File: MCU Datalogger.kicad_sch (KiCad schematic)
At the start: 25 parts, among them U1 24LC1025, U2 24LC1025, U3 DS1337S_, U4 ATMEGA328P-AU, Y1 Crystal, Y2 Crystal

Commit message: Added component values.
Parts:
- C1, C4: value C -> 0.1uF
- C2, C3: value C -> 22pF
- C5: value C_Polarized -> 100nF
- R1, R2: value R -> 4.7K
- R3, R4, R5: value R -> 10K
- R7: value R -> 330
- Y1: value Crystal -> 16 MHz
- Y2: value Crystal -> 32.768 KHz
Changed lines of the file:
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@@
 			)
 		)
-		(property "Value" "R"
+		(property "Value" "10K"
 			(at 106.68 39.3699 0)
 			(effects
@@
 			)
 		)
+		(property "Purpose" ""
+			(at 104.14 38.1 0)
+			(effects
+				(font
+					(size 1.27 1.27)
+				)
+			)
+		)
 		(pin "1"
 		)
@@
 			)
 		)
-		(property "Value" "Crystal"
+		(property "Value" "16 MHz"
 			(at 168.91 52.0699 90)
 			(effects
@@
 			)
 		)
+		(property "Purpose" ""
+			(at 165.1 50.8 0)
+			(effects
+				(font
+					(size 1.27 1.27)
+				)
+			)
+		)
 		(pin "1"
 		)
@@
 			)
 		)
-		(property "Value" "R"
+		(property "Value" "4.7K"
 			(at 99.06 132.0799 0)
 			(effects
@@
 			)
 		)
+		(property "Purpose" ""
+			(at 96.52 130.81 0)
+			(effects
+				(font
+					(size 1.27 1.27)
+				)
+			)
+		)
 		(pin "2"
 		)
@@
 			)
 		)
-		(property "Value" "Crystal"
+		(property "Value" "32.768 KHz"
 			(at 29.21 44.4499 90)
 			(effects
@@
 			)
 		)
+		(property "Purpose" ""
+			(at 25.4 43.18 0)
+			(effects
+				(font
+					(size 1.27 1.27)
+				)
+			)
+		)
 		(pin "1"
 		)
@@
 			)
 		)
-		(property "Value" "R"
+		(property "Value" "330"
 			(at 246.38 57.1499 0)
 			(effects
@@
 			)
 		)
+		(property "Purpose" ""
+			(at 243.84 55.88 0)
+			(effects
+				(font
+					(size 1.27 1.27)
+				)
+			)
+		)
 		(pin "1"
 		)
@@
 			)
 		)
-		(property "Value" "R"
+		(property "Value" "10K"
 			(at 99.06 39.3699 0)
 			(effects
@@
 			)
 		)
+		(property "Purpose" ""
+			(at 96.52 38.1 0)
+			(effects
+				(font
+					(size 1.27 1.27)
+				)
+			)
+		)
 		(pin "1"
 		)
@@
 			)
 		)
-		(property "Value" "C"
+		(property "Value" "0.1uF"
 			(at 118.11 41.9099 0)
 			(effects
@@
 			)
 		)
+		(property "Purpose" ""
+			(at 114.3 40.64 0)
+			(effects
+				(font
+					(size 1.27 1.27)
+				)
+			)
+		)
 		(pin "1"
 		)
@@
 			)
 		)
-		(property "Value" "C_Polarized"
+		(property "Value" "100nF"
 			(at 257.81 32.1309 0)
 			(effects
@@
 			)
 		)
+		(property "Purpose" ""
+			(at 254 31.75 0)
+			(effects
+				(font
+					(size 1.27 1.27)
+				)
+			)
+		)
 		(pin "2"
 		)
@@
 			)
 		)
-		(property "Value" "C"
+		(property "Value" "0.1uF"
 			(at 165.1 15.24 90)
 			(effects
@@
 			)
 		)
+		(property "Purpose" ""
+			(at 165.1 20.32 0)
+			(effects
+				(font
+					(size 1.27 1.27)
+				)
+			)
+		)
 		(pin "2"
 		)
@@
 			)
 		)
-		(property "Value" "R"
+		(property "Value" "10K"
 			(at 166.37 72.39 90)
 			(effects
@@
 			)
 		)
+		(property "Purpose" ""
+			(at 166.37 76.2 0)
+			(effects
+				(font
+					(size 1.27 1.27)
+				)
+			)
+		)
 		(pin "1"
 		)
@@
 			)
 		)
-		(property "Value" "R"
+		(property "Value" "4.7K"
 			(at 106.68 132.0799 0)
 			(effects
@@
 			)
 		)
+		(property "Purpose" ""
+			(at 104.14 130.81 0)
+			(effects
+				(font
+					(size 1.27 1.27)
+				)
+			)
+		)
 		(pin "1"
 		)
@@
 			)
 		)
-		(property "Value" "C"
+		(property "Value" "22pF"
 			(at 151.13 50.7999 0)
 			(effects
@@
 			)
 		)
+		(property "Purpose" ""
+			(at 147.32 49.53 0)
+			(effects
+				(font
+					(size 1.27 1.27)
+				)
+			)
+		)
 		(pin "1"
 		)
@@
 			)
 		)
-		(property "Value" "C"
+		(property "Value" "22pF"
 			(at 151.13 68.5799 0)
 			(effects
@@
 			)
 		)
+		(property "Purpose" ""
+			(at 147.32 67.31 0)
+			(effects
+				(font
+					(size 1.27 1.27)
+				)
+			)
+		)

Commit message: Completed symbol-footprint associations.
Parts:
- BT1: footprint (none) -> Connector_PinHeader_2.54mm:PinHeader_1x01_P2.54mm_Vertical
- C1, C2, C3, C4, C5: footprint (none) -> Capacitor_SMD:C_0805_2012Metric
- D1, D2: footprint (none) -> LED_SMD:LED_0805_2012Metric
- H1, H2, H3, H4: footprint (none) -> MountingHole:MountingHole_2.1mm
- R1, R2, R3, R4, R5, R7: footprint (none) -> Resistor_SMD:R_0805_2012Metric
- R6: value R -> 330; footprint (none) -> Resistor_SMD:R_0805_2012Metric
- U1, U2: footprint (none) -> Package_SO:SSOP-8_5.25x5.24mm_P1.27mm
- U3: footprint DS1337S_:SOIC127P600X175-8N -> MCU Datalogger:SOIC127P600X175-8N
- U4: footprint ATMEGA328P-AU:QFP80P900X900X120-32N -> MCU Datalogger:QFP80P900X900X120-32N
- Y1, Y2: footprint (none) -> Crystal:Crystal_SMD_5032-2Pin_5.0x3.2mm_HandSoldering
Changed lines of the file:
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@@
 			)
 		)
-		(property "Footprint" ""
+		(property "Footprint" "Resistor_SMD:R_0805_2012Metric"
 			(at 102.362 38.1 90)
 			(effects
@@
 			)
 		)
-		(property "Footprint" ""
+		(property "Footprint" "MountingHole:MountingHole_2.1mm"
 			(at 208.28 134.62 0)
 			(effects
@@
 			)
 		)
-		(property "Footprint" "ATMEGA328P-AU:QFP80P900X900X120-32N"
+		(property "Footprint" "MCU Datalogger:QFP80P900X900X120-32N"
 			(at 210.82 48.26 0)
 			(effects
@@
 			)
 		)
-		(property "Footprint" ""
+		(property "Footprint" "Crystal:Crystal_SMD_5032-2Pin_5.0x3.2mm_HandSoldering"
 			(at 165.1 50.8 0)
 			(effects
@@
 			)
 		)
-		(property "Footprint" ""
+		(property "Footprint" "Resistor_SMD:R_0805_2012Metric"
 			(at 94.742 130.81 90)
 			(effects
@@
 			)
 		)
-		(property "Footprint" ""
+		(property "Footprint" "Crystal:Crystal_SMD_5032-2Pin_5.0x3.2mm_HandSoldering"
 			(at 25.4 43.18 0)
 			(effects
@@
 			)
 		)
-		(property "Footprint" ""
+		(property "Footprint" "Resistor_SMD:R_0805_2012Metric"
 			(at 242.062 55.88 90)
 			(effects
@@
 			)
 		)
-		(property "Value" "R"
+		(property "Value" "330"
 			(at 148.59 29.21 90)
 			(effects
@@
 			)
 		)
-		(property "Footprint" ""
+		(property "Footprint" "Resistor_SMD:R_0805_2012Metric"
 			(at 148.59 34.798 90)
 			(effects
@@
 			)
 		)
+		(property "Purpose" ""
+			(at 148.59 33.02 0)
+			(effects
+				(font
+					(size 1.27 1.27)
+				)
+			)
+		)
 		(pin "2"
 		)
@@
 			)
 		)
-		(property "Footprint" "DS1337S_:SOIC127P600X175-8N"
+		(property "Footprint" "MCU Datalogger:SOIC127P600X175-8N"
 			(at 66.04 43.18 0)
 			(effects
@@
 			)
 		)
-		(property "Footprint" ""
+		(property "Footprint" "Resistor_SMD:R_0805_2012Metric"
 			(at 94.742 38.1 90)
 			(effects
@@
 			)
 		)
-		(property "Footprint" ""
+		(property "Footprint" "Capacitor_SMD:C_0805_2012Metric"
 			(at 115.2652 44.45 0)
 			(effects
@@
 			)
 		)
-		(property "Footprint" ""
+		(property "Footprint" "MountingHole:MountingHole_2.1mm"
 			(at 208.28 139.7 0)
 			(effects
@@
 			)
 		)
-		(property "Footprint" ""
+		(property "Footprint" "Capacitor_SMD:C_0805_2012Metric"
 			(at 254.9652 35.56 0)
 			(effects
@@
 			)
 		)
-		(property "Footprint" ""
+		(property "Footprint" "Capacitor_SMD:C_0805_2012Metric"
 			(at 168.91 19.3548 0)
 			(effects
@@
 			)
 		)
-		(property "Footprint" ""
+		(property "Footprint" "Resistor_SMD:R_0805_2012Metric"
 			(at 166.37 74.422 90)
 			(effects
@@
 			)
 		)
-		(property "Footprint" ""
+		(property "Footprint" "MountingHole:MountingHole_2.1mm"
 			(at 208.28 124.46 0)
 			(effects
@@
 			)
 		)
-		(property "Footprint" ""
+		(property "Footprint" "Package_SO:SSOP-8_5.25x5.24mm_P1.27mm"
 			(at 71.12 129.54 0)
 			(effects
@@
 			)
 		)
-		(property "Footprint" ""
+		(property "Footprint" "LED_SMD:LED_0805_2012Metric"
 			(at 243.84 40.64 0)
 			(effects
@@
 			)
 		)
-		(property "Footprint" ""
+		(property "Footprint" "MountingHole:MountingHole_2.1mm"
 			(at 208.28 129.54 0)
 			(effects
@@
 			)
 		)
-		(property "Footprint" ""
+		(property "Footprint" "Connector_PinHeader_2.54mm:PinHeader_1x01_P2.54mm_Vertical"
 			(at 271.78 28.956 90)
 			(effects
@@
 			)
 		)
-		(property "Footprint" ""
+		(property "Footprint" "Resistor_SMD:R_0805_2012Metric"
 			(at 102.362 130.81 90)
 			(effects
@@
 			)
 		)
-		(property "Footprint" ""
+		(property "Footprint" "Capacitor_SMD:C_0805_2012Metric"
 			(at 148.2852 53.34 0)
 			(effects
@@
 			)
 		)
-		(property "Footprint" ""
+		(property "Footprint" "Package_SO:SSOP-8_5.25x5.24mm_P1.27mm"
 			(at 43.18 129.54 0)
 			(effects
@@
 			)
 		)
-		(property "Footprint" ""
+		(property "Footprint" "Capacitor_SMD:C_0805_2012Metric"
 			(at 148.2852 71.12 0)
 			(effects
@@
 			)
 		)
-		(property "Footprint" ""
+		(property "Footprint" "LED_SMD:LED_0805_2012Metric"
 			(at 167.64 33.02 0)
 			(effects

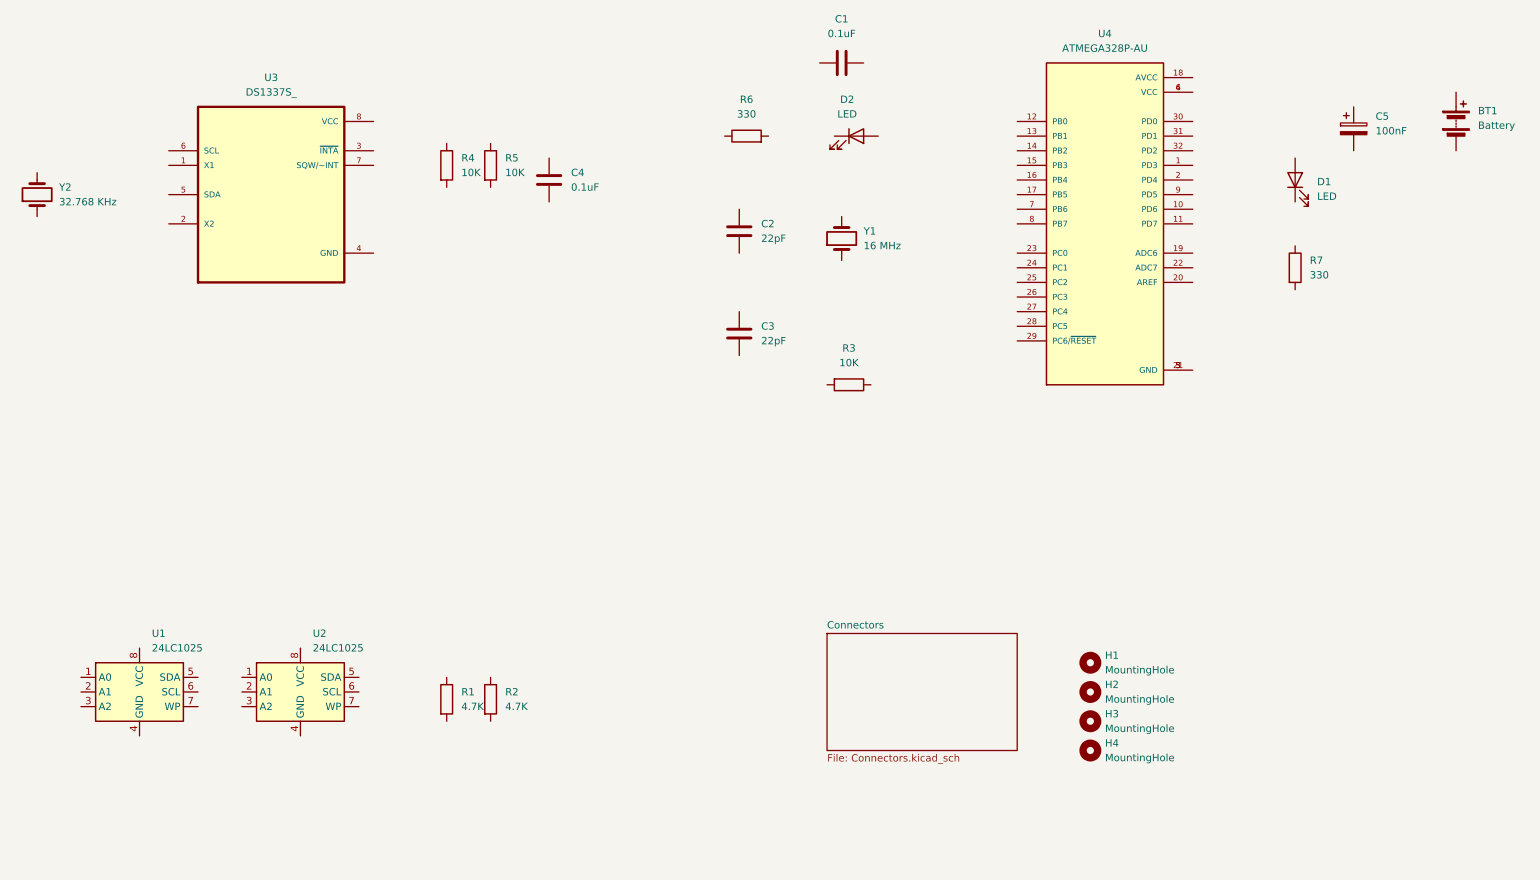
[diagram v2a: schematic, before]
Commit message: Completed wiring of main sheet.
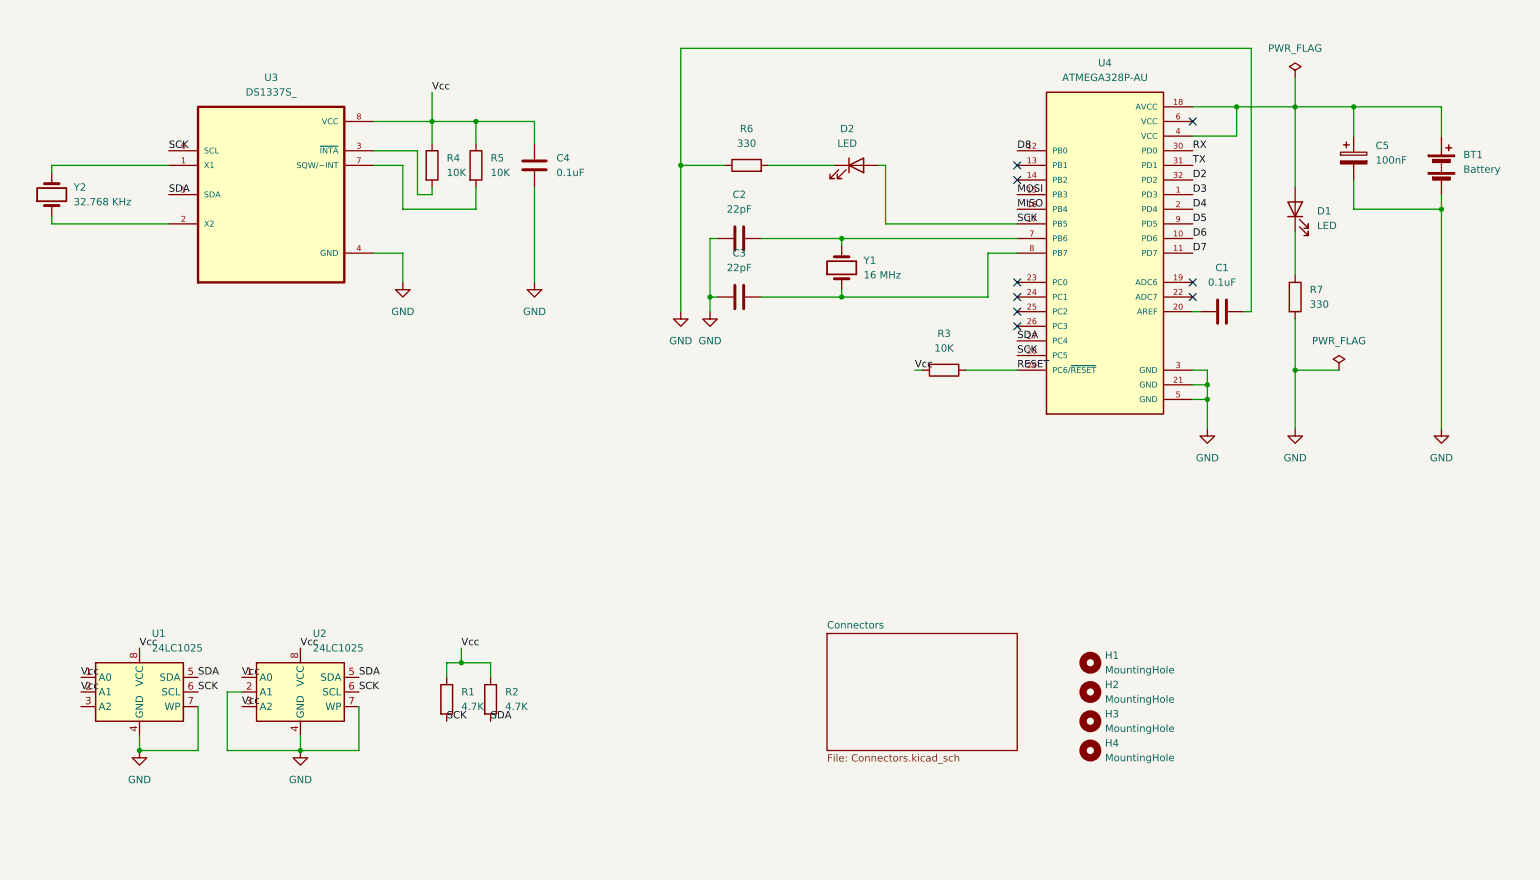
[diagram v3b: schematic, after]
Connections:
- net Vcc: now reaches R5.1
- net Vcc: now also C4.1, R1.1, R2.1, R3.2, R4.1, U1.1 (A0), U1.2 (A1), U1.8 (VCC), U2.1 (A0), U2.3 (A2), U2.8 (VCC), U3.8 (VCC)
- net at R5.2: now also U3.7 (SQW/~INT)
- net D3: now reaches U4.1 (PD3)
- net D6: now reaches U4.10 (PD6)
- net D7: now reaches U4.11 (PD7)
- net D8: now reaches U4.12 (PB0)
- net MOSI: now reaches U4.15 (PB3)
- net MISO: now reaches U4.16 (PB4)
- net SCK: now reaches U4.17 (PB5)
- net SCK: now also D2.2 (A), R1.2, U1.6 (SCL), U2.6 (SCL), U3.6 (SCL), U4.28 (PC5)
- net at U4.18 (AVCC): now also BT1.1 (+), C5.1, D1.2 (A), U4.4 (VCC)
- net D4: now reaches U4.2 (PD4)
- net at U4.20 (AREF): now also C1.1
- net GND: now reaches U4.21 (GND), U4.3 (GND), U4.5 (GND)
- net GND: now also BT1.2 (-), C1.2, C2.1, C3.1, C4.2, C5.2, R6.1, R7.2, U1.4 (GND), U1.7 (WP), U2.2 (A1), U2.4 (GND), U2.7 (WP), U3.4 (GND)
- net SDA: now reaches U4.27 (PC4)
- net SDA: now also R2.2, U1.5 (SDA), U2.5 (SDA), U3.5 (SDA)
- net RESET: now reaches U4.29 (PC6/~{RESET})
- net RESET: now also R3.1
- net RX: now reaches U4.30 (PD0)
- net TX: now reaches U4.31 (PD1)
- net D2: now reaches U4.32 (PD2)
- net at U4.6 (VCC): no longer U4.4 (VCC)
- net at U4.7 (PB6): now also C2.2, Y1.2
- net at U4.8 (PB7): now also C3.2, Y1.1
- net D5: now reaches U4.9 (PD5)
- net at Y2.1: now also U3.2 (X2)
- net at Y2.2: now also U3.1 (X1)
- net at R7.1: now also D1.1 (K)
- net at R6.2: now also D2.1 (K)
- net at U3.3 (~{INTA}): now also R4.2
- no-connect marks 0 -> 9
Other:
- moved on the sheet: BT1, C1, C2, C3, C4, C5, D1, D2, R3, R4, R5, R6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

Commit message: Completed wiring in the second sheet.
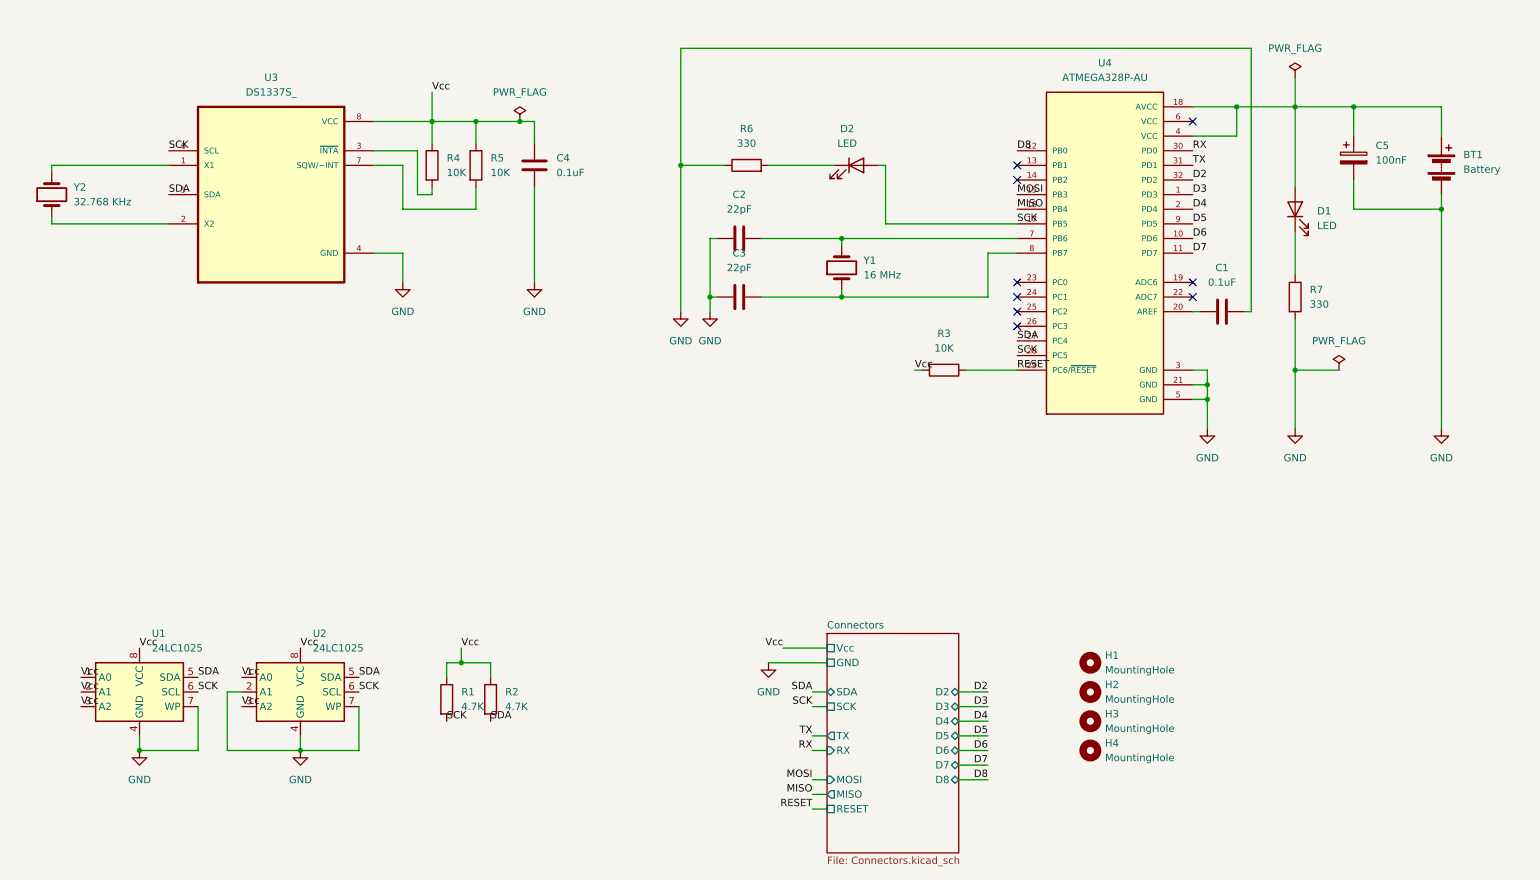
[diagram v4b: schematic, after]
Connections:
- net Vcc: now also U1.3 (A2)
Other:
- sheet Connectors ports: added D2, D3, D4, D5, D6, D7, D8, GND, MISO, MOSI, RESET, RX, SCK, SDA, TX, Vcc; removed none

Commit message: Completed comments.
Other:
- note added: "EEPROM"
- note added: "MCU"
- note added: "Mounting"
- note added: "Real Time Clock"
- moved on the sheet: BT1, C1, C2, C3, C4, C5, D1, D2, H1, H2, H3, H4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

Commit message: Setup Pcbnew.
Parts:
- BT1: footprint Connector_PinHeader_2.54mm:PinHeader_1x01_P2.54mm_Vertical -> Connector_PinHeader_2.54mm:PinHeader_1x02_P2.54mm_Vertical
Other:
- moved on the sheet: R1, R2
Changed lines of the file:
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@@
 	(wire
 		(pts
-			(xy 170.18 93.98) (xy 171.45 93.98)
+			(xy 167.64 93.98) (xy 171.45 93.98)
 		)
 		(stroke
@@
 	(wire
 		(pts
-			(xy 101.6 99.06) (xy 101.6 101.6)
+			(xy 101.6 99.06) (xy 101.6 100.33)
 		)
 		(stroke
@@
 	(wire
 		(pts
-			(xy 101.6 111.76) (xy 101.6 109.22)
+			(xy 101.6 110.49) (xy 101.6 107.95)
 		)
 		(stroke
@@
 	(wire
 		(pts
-			(xy 93.98 101.6) (xy 93.98 99.06)
+			(xy 91.44 100.33) (xy 91.44 99.06)
 		)
 		(stroke
@@
 	(wire
 		(pts
-			(xy 93.98 99.06) (xy 96.52 99.06)
+			(xy 91.44 99.06) (xy 96.52 99.06)
 		)
 		(stroke
@@
 	(wire
 		(pts
-			(xy 93.98 111.76) (xy 93.98 109.22)
+			(xy 91.44 110.49) (xy 91.44 107.95)
 		)
 		(stroke
@@
 	)
 	(label "SCK"
-		(at 93.98 111.76 0)
+		(at 91.44 110.49 0)
 		(effects
 			(font
@@
 	)
 	(label "SDA"
-		(at 101.6 111.76 0)
+		(at 101.6 110.49 0)
 		(effects
 			(font
@@
 	)
 	(label "Vcc"
-		(at 170.18 93.98 0)
+		(at 167.64 93.98 0)
 		(effects
 			(font
@@
 		(polyline
 			(pts
-				(xy 177.8 119.38) (xy 198.12 119.38) (xy 198.12 149.86) (xy 177.8 149.86)
+				(xy 127 35.56) (xy 274.32 35.56) (xy 274.32 111.76) (xy 127 111.76)
 			)
 			(stroke
@@
 		(polyline
 			(pts
-				(xy 127 35.56) (xy 274.32 35.56) (xy 274.32 111.76) (xy 127 111.76)
+				(xy 177.8 119.38) (xy 198.12 119.38) (xy 198.12 149.86) (xy 177.8 149.86)
 			)
 			(stroke
@@
 	(symbol
 		(lib_id "Device:R")
-		(at 93.98 105.41 0)
+		(at 91.44 104.14 0)
 		(unit 1)
 		(exclude_from_sim no)
@@
 		(fields_autoplaced yes)
 		(property "Reference" "R1"
-			(at 96.52 104.1399 0)
+			(at 93.98 102.8699 0)
 			(effects
 				(font
@@
 		)
 		(property "Value" "4.7K"
-			(at 96.52 106.6799 0)
+			(at 93.98 105.4099 0)
 			(effects
 				(font
@@
 		)
 		(property "Footprint" "Resistor_SMD:R_0805_2012Metric"
-			(at 92.202 105.41 90)
+			(at 89.662 104.14 90)
 			(effects
 				(font
@@
 		)
 		(property "Datasheet" "~"
-			(at 93.98 105.41 0)
+			(at 91.44 104.14 0)
 			(effects
 				(font
@@
 		)
 		(property "Description" "Resistor"
-			(at 93.98 105.41 0)
+			(at 91.44 104.14 0)
 			(effects
 				(font
@@
 		)
 		(property "Purpose" ""
-			(at 93.98 105.41 0)
+			(at 91.44 104.14 0)
 			(effects
 				(font
@@
 			)
 		)
-		(property "Footprint" "Connector_PinHeader_2.54mm:PinHeader_1x01_P2.54mm_Vertical"
+		(property "Footprint" "Connector_PinHeader_2.54mm:PinHeader_1x02_P2.54mm_Vertical"
 			(at 261.62 56.896 90)
 			(effects
@@
 	(symbol
 		(lib_id "Device:R")
-		(at 101.6 105.41 0)
+		(at 101.6 104.14 0)
 		(unit 1)
 		(exclude_from_sim no)
@@
 		(fields_autoplaced yes)
 		(property "Reference" "R2"
-			(at 104.14 104.1399 0)
+			(at 104.14 102.8699 0)
 			(effects
 				(font
@@
 		)
 		(property "Value" "4.7K"
-			(at 104.14 106.6799 0)
+			(at 104.14 105.4099 0)
 			(effects
 				(font
@@
 		)
 		(property "Footprint" "Resistor_SMD:R_0805_2012Metric"
-			(at 99.822 105.41 90)
+			(at 99.822 104.14 90)
 			(effects
 				(font
@@
 		)
 		(property "Datasheet" "~"
-			(at 101.6 105.41 0)
+			(at 101.6 104.14 0)
 			(effects
 				(font
@@
 		)
 		(property "Description" "Resistor"
-			(at 101.6 105.41 0)
+			(at 101.6 104.14 0)
 			(effects
 				(font
@@
 		)
 		(property "Purpose" ""
-			(at 101.6 105.41 0)
+			(at 101.6 104.14 0)
 			(effects
 				(font
